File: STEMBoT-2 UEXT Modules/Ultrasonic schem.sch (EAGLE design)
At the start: 4 parts, among them U1 HC-SR04

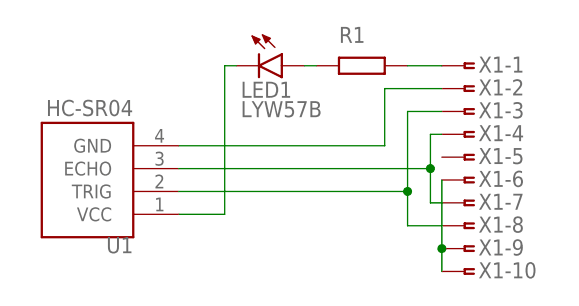
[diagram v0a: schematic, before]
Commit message: I am a little wary off all this stuff in here. I went ahead and added an ultrasonic schem in here. Dont know why it wasnt in before.
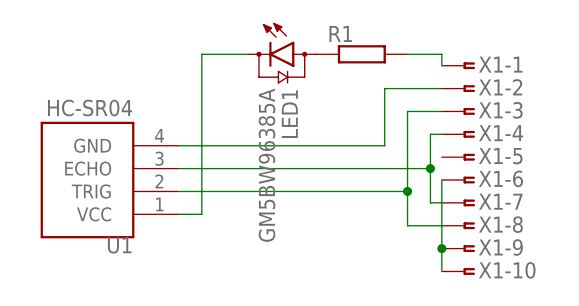
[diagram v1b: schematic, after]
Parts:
- LED1: value LYW57B -> GM5BW96385A; device led:LYW57B -> led:GM5BW96385A
- R1: device ngspice-simulation:R -> resistor-shunt:SMK
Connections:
- removed net N$1 (its old number): R1.2, X1-1.1
- new net N$8: LED1.A, R1.2
- net N$2: now also X1-1.1; no longer LED1.A
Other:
- moved on the sheet: R1
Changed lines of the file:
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@@
 <layers>
 <layer number="1" name="Top" color="4" fill="1" visible="no" active="no"/>
+<layer number="2" name="Route2" color="1" fill="3" visible="no" active="no"/>
+<layer number="3" name="Route3" color="4" fill="3" visible="no" active="no"/>
+<layer number="4" name="Route4" color="1" fill="4" visible="no" active="no"/>
+<layer number="5" name="Route5" color="4" fill="4" visible="no" active="no"/>
+<layer number="6" name="Route6" color="1" fill="8" visible="no" active="no"/>
+<layer number="7" name="Route7" color="4" fill="8" visible="no" active="no"/>
+<layer number="8" name="Route8" color="1" fill="2" visible="no" active="no"/>
+<layer number="9" name="Route9" color="4" fill="2" visible="no" active="no"/>
+<layer number="10" name="Route10" color="1" fill="7" visible="no" active="no"/>
+<layer number="11" name="Route11" color="4" fill="7" visible="no" active="no"/>
+<layer number="12" name="Route12" color="1" fill="5" visible="no" active="no"/>
+<layer number="13" name="Route13" color="4" fill="5" visible="no" active="no"/>
+<layer number="14" name="Route14" color="1" fill="6" visible="no" active="no"/>
+<layer number="15" name="Route15" color="4" fill="6" visible="no" active="no"/>
 <layer number="16" name="Bottom" color="1" fill="1" visible="no" active="no"/>
 <layer number="17" name="Pads" color="2" fill="1" visible="no" active="no"/>
@@
 </classes>
 <parts>
-<part name="LED1" library="led" library_urn="urn:adsk.eagle:library:259" deviceset="*W57B" device="" package3d_urn="urn:adsk.eagle:package:15859/1" technology="LY"/>
-<part name="R1" library="ngspice-simulation" library_urn="urn:adsk.eagle:library:527439" deviceset="R" device=""/>
 <part name="X1" library="con-amp" library_urn="urn:adsk.eagle:library:127" deviceset="FSIDE-10" device="" package3d_urn="urn:adsk.eagle:package:8081495/1"/>
 <part name="U1" library="HC-SR04" deviceset="HC-SR04" device=""/>
+<part name="LED1" library="led" library_urn="urn:adsk.eagle:library:259" deviceset="GM5BW96385A" device="" package3d_urn="urn:adsk.eagle:package:15867/1"/>
+<part name="R1" library="resistor-shunt" library_urn="urn:adsk.eagle:library:346" deviceset="SMK" device="" package3d_urn="urn:adsk.eagle:package:25215/1"/>
 </parts>
 <sheets>
@@
 </plain>
 <instances>
-<instance part="LED1" gate="G$1" x="107.95" y="77.47" smashed="yes" rot="R270">
-<attribute name="NAME" x="103.378" y="73.914" size="1.778" layer="95"/>
-<attribute name="VALUE" x="103.378" y="71.755" size="1.778" layer="96"/>
-</instance>
-<instance part="R1" gate="G$1" x="116.84" y="77.47" smashed="yes">
-<attribute name="NAME" x="114.3" y="80.01" size="1.778" layer="95"/>
-<attribute name="VALUE" x="114.3" y="73.66" size="1.778" layer="96"/>
-</instance>
 <instance part="X1" gate="-1" x="128.27" y="77.47" smashed="yes">
 <attribute name="NAME" x="129.794" y="76.708" size="1.778" layer="95"/>
@@
 <attribute name="NAME" x="91.44" y="58.4187" size="1.778459375" layer="95" rot="R180"/>
 <attribute name="VALUE" x="91.44" y="73.663" size="1.77851875" layer="96" rot="R180"/>
+</instance>
+<instance part="LED1" gate="B" x="109.22" y="78.74" smashed="yes" rot="R270">
+<attribute name="NAME" x="107.95" y="74.93" size="1.778" layer="95" rot="R270"/>
+<attribute name="VALUE" x="105.41" y="74.93" size="1.778" layer="96" rot="R270"/>
+</instance>
+<instance part="R1" gate="G$1" x="116.84" y="78.74" smashed="yes">
+<attribute name="NAME" x="113.03" y="80.1116" size="1.778" layer="95"/>
+<attribute name="VALUE" x="113.03" y="75.819" size="1.778" layer="96"/>
 </instance>
 </instances>
@@
 </busses>
 <nets>
-<net name="N$1" class="0">
-<segment>
-<pinref part="X1" gate="-1" pin="1"/>
-<pinref part="R1" gate="G$1" pin="2"/>
-<wire x1="125.73" y1="77.47" x2="121.92" y2="77.47" width="0.1524" layer="91"/>
-</segment>
-</net>
-<net name="N$2" class="0">
-<segment>
-<pinref part="R1" gate="G$1" pin="1"/>
-<wire x1="111.76" y1="77.47" x2="110.49" y2="77.47" width="0.1524" layer="91"/>
-<pinref part="LED1" gate="G$1" pin="A"/>
-</segment>
-</net>
-<net name="N$3" class="0">
-<segment>
-<pinref part="U1" gate="G$1" pin="VCC"/>
-<wire x1="96.52" y1="60.96" x2="101.6" y2="60.96" width="0.1524" layer="91"/>
-<pinref part="LED1" gate="G$1" pin="C"/>
-<wire x1="101.6" y1="60.96" x2="101.6" y2="77.47" width="0.1524" layer="91"/>
-<wire x1="101.6" y1="77.47" x2="102.87" y2="77.47" width="0.1524" layer="91"/>
-</segment>
-</net>
 <net name="N$5" class="0">
 <segment>
@@
 <wire x1="125.73" y1="54.61" x2="125.73" y2="57.15" width="0.1524" layer="91"/>
 <junction x="125.73" y="57.15"/>
+</segment>
+</net>
+<net name="N$8" class="0">
+<segment>
+<pinref part="LED1" gate="B" pin="A"/>
+<pinref part="R1" gate="G$1" pin="2"/>
+</segment>
+</net>
+<net name="N$1" class="0">
+<segment>
+<pinref part="U1" gate="G$1" pin="VCC"/>
+<wire x1="96.52" y1="60.96" x2="99.06" y2="60.96" width="0.1524" layer="91"/>
+<wire x1="99.06" y1="60.96" x2="99.06" y2="78.74" width="0.1524" layer="91"/>
+<pinref part="LED1" gate="B" pin="C"/>
+<wire x1="99.06" y1="78.74" x2="104.14" y2="78.74" width="0.1524" layer="91"/>
+</segment>
+</net>
+<net name="N$2" class="0">
+<segment>
+<pinref part="R1" gate="G$1" pin="1"/>
+<pinref part="X1" gate="-1" pin="1"/>
+<wire x1="121.92" y1="78.74" x2="125.73" y2="78.74" width="0.1524" layer="91"/>
+<wire x1="125.73" y1="78.74" x2="125.73" y2="77.47" width="0.1524" layer="91"/>
 </segment>
 </net>
@@
 packages will not be understood (or retained) with this version.
 </note>
-<note version="8.4" severity="warning">
-Since Version 8.4, EAGLE supports properties for SPICE simulation.
-Probes in schematics and SPICE mapping objects found in parts and library devices
-will not be understood with this version. Update EAGLE to the latest version
-for full support of SPICE simulation.
-</note>
 </compatibility>
